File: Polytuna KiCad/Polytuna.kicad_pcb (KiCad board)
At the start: 2 copper layers, 114.3 x 64.8 mm, 73 parts, among them IC1 AP7313-33SAG-7, J1 Barrel_Jack, J2 Conn_01x02, J3 Conn_01x02, J4 Conn_01x04, J5 Conn_01x02, SW1 SW_Push, SW2 SW_Push, SW3 SW_Push, SW4 SW_TPDT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

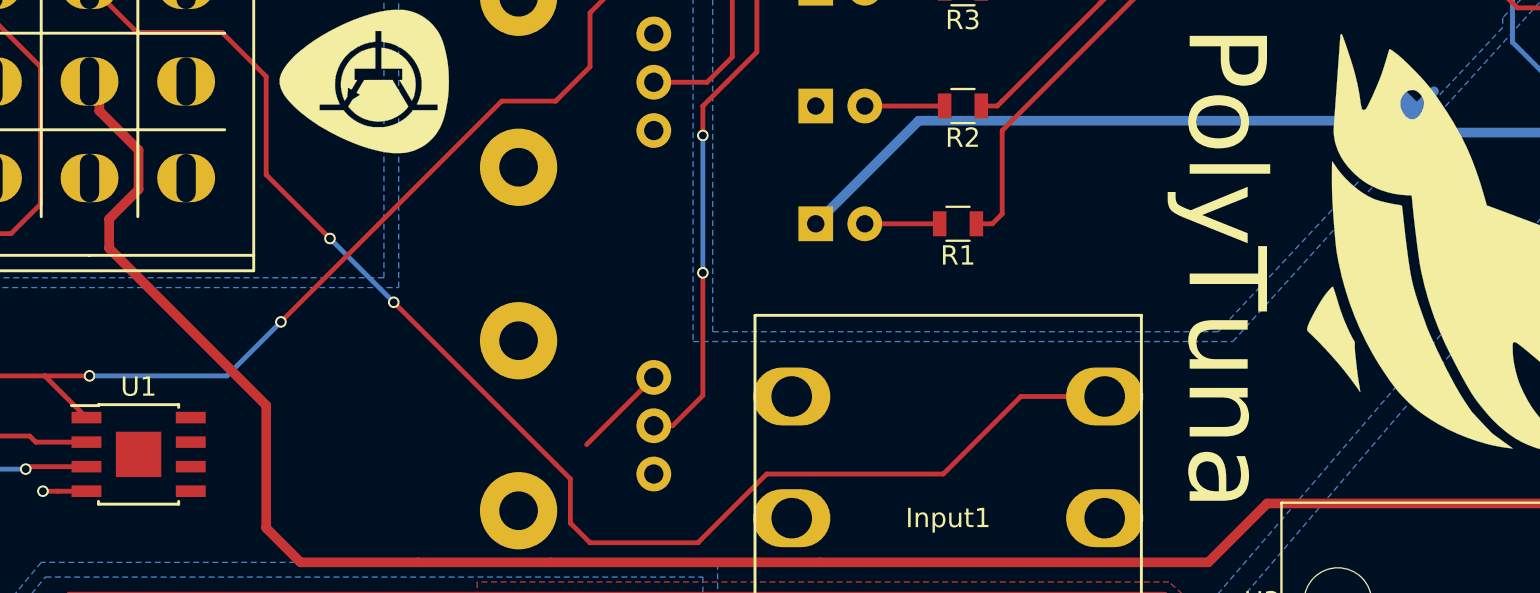
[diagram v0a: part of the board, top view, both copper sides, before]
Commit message: Changed OP's footprint
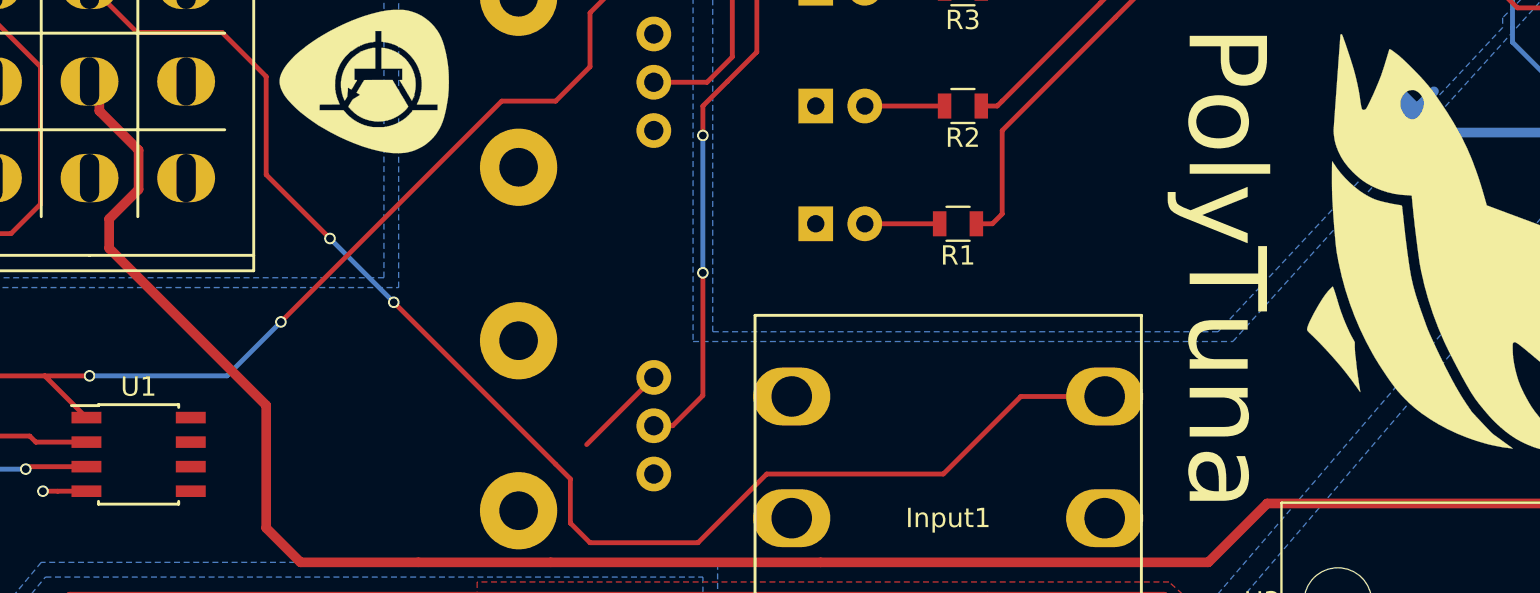
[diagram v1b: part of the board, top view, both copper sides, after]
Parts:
- U1: footprint Housings_SOIC:SOIC-8-1EP_3.9x4.9mm_Pitch1.27mm -> Housings_SOIC:SOIC-8_3.9x4.9mm_Pitch1.27mm
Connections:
- BOARD1 pad 12: (no net) -> Net-(BOARD1-Pad12)
- BOARD1 pad 14: (no net) -> Net-(BOARD1-Pad14)
- BOARD1 pad 19: (no net) -> Net-(BOARD1-Pad19)
- BOARD1 pad 2: (no net) -> Net-(BOARD1-Pad2)
- BOARD1 pad 22: (no net) -> Net-(BOARD1-Pad22)
- BOARD1 pad 23: (no net) -> Net-(BOARD1-Pad23)
- BOARD1 pad 3: (no net) -> Net-(BOARD1-Pad3)
- BOARD1 pad 4: (no net) -> Net-(BOARD1-Pad4)
- SW4 pad 12: (no net) -> Net-(SW4-Pad12)
- SW4 pad 13: (no net) -> Net-(SW4-Pad13)
- U2 pad 11: (no net) -> Net-(U2-Pad11)
- U2 pad 13: (no net) -> Net-(U2-Pad13)
- U2 pad 15: (no net) -> Net-(U2-Pad15)
- U2 pad 16: (no net) -> Net-(U2-Pad16)
- U2 pad 18: (no net) -> Net-(U2-Pad18)
- U2 pad 2: (no net) -> Net-(U2-Pad2)
- U2 pad 4: (no net) -> Net-(U2-Pad4)
- U2 pad 6: (no net) -> Net-(U2-Pad6)
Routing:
- net GND: track 209.7 -> 176.2 mm
